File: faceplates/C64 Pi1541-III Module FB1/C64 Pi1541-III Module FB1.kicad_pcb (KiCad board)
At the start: 2 copper layers, 100 x 100 mm, 7 parts, among them M1 Mounting, M2 Mounting, M3 Mounting, M4 Mounting

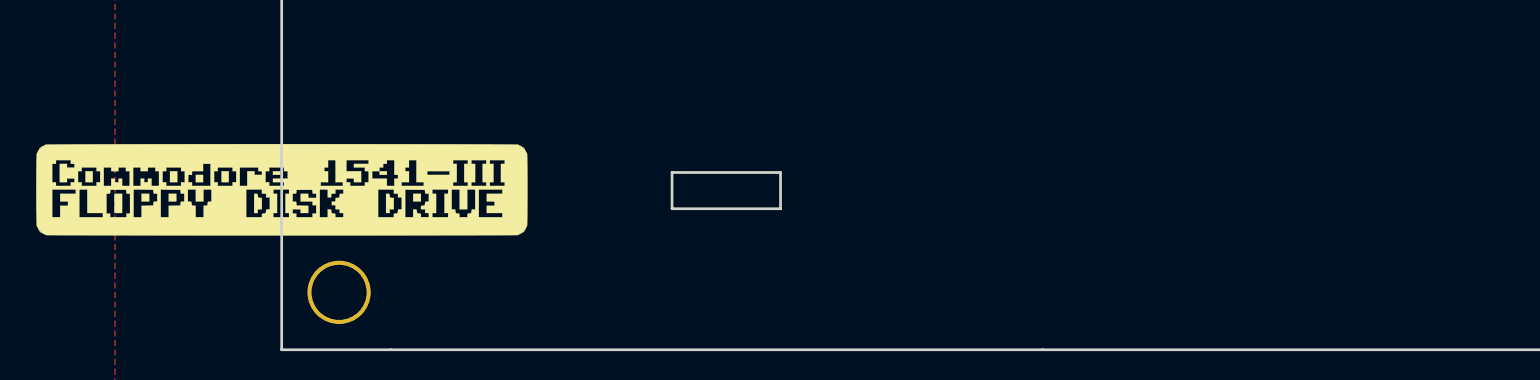
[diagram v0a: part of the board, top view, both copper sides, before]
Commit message: Tweak footprint placement
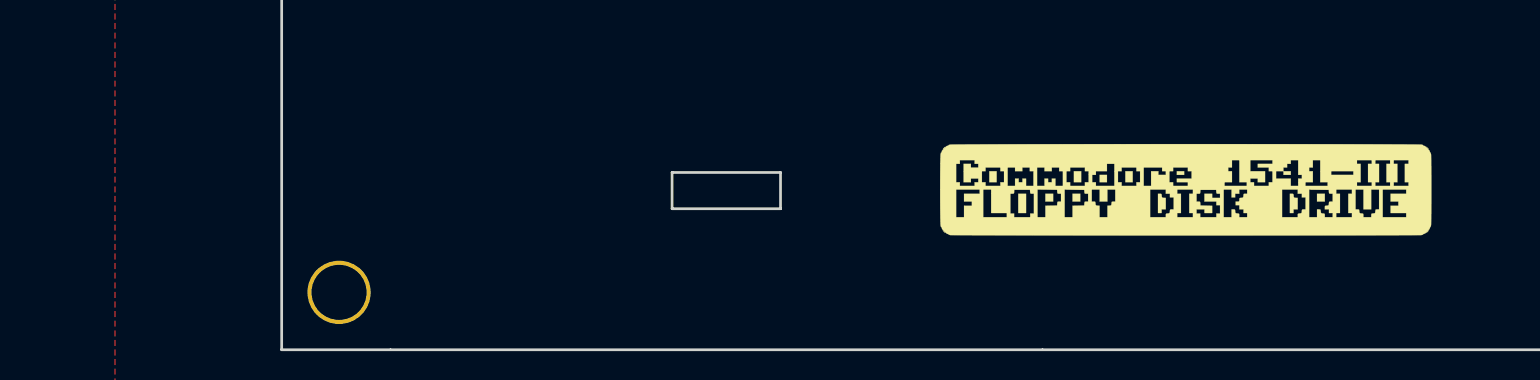
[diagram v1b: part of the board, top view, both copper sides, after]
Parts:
- moved G*** 50.0 mm to (120.2, 145.8)
